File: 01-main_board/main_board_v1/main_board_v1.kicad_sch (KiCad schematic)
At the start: 2 parts, among them J1 Ethernet and USB, J4 DB44 (Analog | Digital)

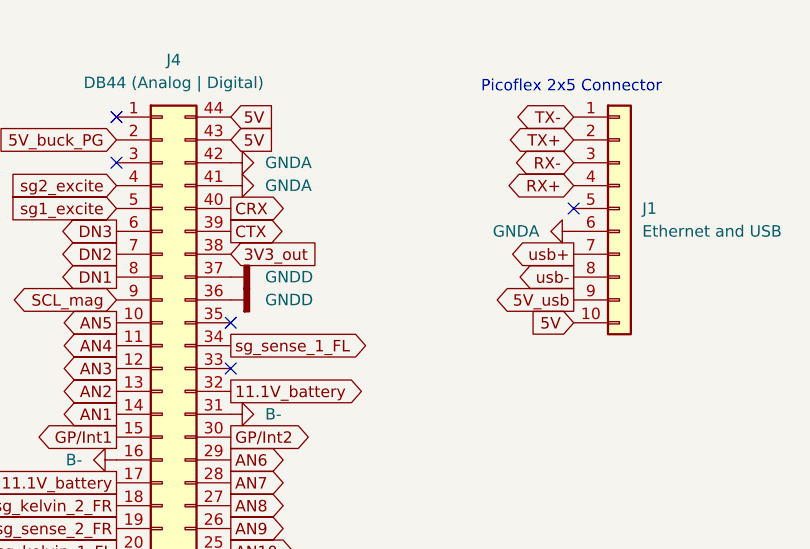
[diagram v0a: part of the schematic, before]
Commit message: Added main board footprint library
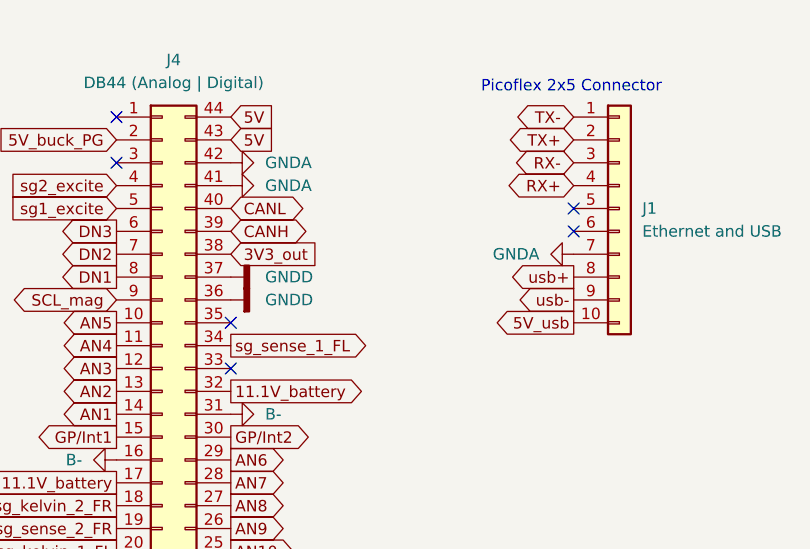
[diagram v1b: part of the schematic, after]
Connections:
- net 5V: no longer J1.10 (Pin_10)
- net 5V_usb: now also J1.10 (Pin_10); no longer J1.9 (Pin_9)
- net GNDA: now also J1.7 (Pin_7); no longer J1.6 (Pin_6)
- net usb+: now also J1.8 (Pin_8); no longer J1.7 (Pin_7)
- net usb-: now also J1.9 (Pin_9); no longer J1.8 (Pin_8)
- net CRX renamed CANL
- net CTX renamed CANH
- no-connect marks 5 -> 6
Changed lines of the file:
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@@
+	)
+	(no_connect
+		(at 111.76 43.18)
 	)
 	(no_connect
@@
 	)
 	(no_connect
+		(at 111.76 45.72)
+	)
+	(no_connect
 		(at 73.66 60.96)
 	)
@@
 		(at 60.96 38.1)
 	)
-	(no_connect
-		(at 111.76 43.18)
-	)
 	(global_label "AN7"
 		(shape output)
@@
 				)
 				(justify right)
+				(hide yes)
+			)
+		)
+	)
+	(global_label "CANL"
+		(shape bidirectional)
+		(at 73.66 43.18 0)
+		(fields_autoplaced yes)
+		(effects
+			(font
+				(size 1.27 1.27)
+			)
+			(justify left)
+		)
+		(property "Intersheetrefs" "${INTERSHEET_REFS}"
+			(at 82.4737 43.18 0)
+			(effects
+				(font
+					(size 1.27 1.27)
+				)
+				(justify left)
+				(hide yes)
+			)
+		)
+	)
+	(global_label "CANH"
+		(shape bidirectional)
+		(at 73.66 45.72 0)
+		(fields_autoplaced yes)
+		(effects
+			(font
+				(size 1.27 1.27)
+			)
+			(justify left)
+		)
+		(property "Intersheetrefs" "${INTERSHEET_REFS}"
+			(at 82.7761 45.72 0)
+			(effects
+				(font
+					(size 1.27 1.27)
+				)
+				(justify left)
 				(hide yes)
 			)
@@
 		)
 	)
-	(global_label "usb+"
-		(shape output)
-		(at 111.76 48.26 180)
-		(fields_autoplaced yes)
-		(effects
-			(font
-				(face "KiCad Font")
-				(size 1.27 1.27)
-			)
-			(justify right)
-		)
-		(property "Intersheetrefs" "${INTERSHEET_REFS}"
-			(at 103.8763 48.26 0)
-			(effects
-				(font
-					(size 1.27 1.27)
-				)
-				(justify right)
-				(hide yes)
-			)
-		)
-	)
 	(global_label "linpot_2_FR"
 		(shape output)
@@
 		)
 	)
-	(global_label "5V_usb"
-		(shape output)
-		(at 111.76 53.34 180)
-		(fields_autoplaced yes)
-		(effects
-			(font
-				(size 1.27 1.27)
-			)
-			(justify right)
-		)
-		(property "Intersheetrefs" "${INTERSHEET_REFS}"
-			(at 102.183 53.34 0)
-			(effects
-				(font
-					(size 1.27 1.27)
-				)
-				(justify right)
-				(hide yes)
-			)
-		)
-	)
 	(global_label "DN5"
 		(shape input)
@@
 		)
 	)
+	(global_label "usb+"
+		(shape output)
+		(at 111.76 50.8 180)
+		(fields_autoplaced yes)
+		(effects
+			(font
+				(face "KiCad Font")
+				(size 1.27 1.27)
+			)
+			(justify right)
+		)
+		(property "Intersheetrefs" "${INTERSHEET_REFS}"
+			(at 103.8763 50.8 0)
+			(effects
+				(font
+					(size 1.27 1.27)
+				)
+				(justify right)
+				(hide yes)
+			)
+		)
+	)
 	(global_label "11.1V_battery"
 		(shape output)
@@
 		)
 	)
-	(global_label "5V"
-		(shape input)
-		(at 111.76 55.88 180)
-		(fields_autoplaced yes)
-		(effects
-			(font
-				(size 1.27 1.27)
-			)
-			(justify right)
-		)
-		(property "Intersheetrefs" "${INTERSHEET_REFS}"
-			(at 106.4767 55.88 0)
-			(effects
-				(font
-					(size 1.27 1.27)
-				)
-				(justify right)
-				(hide yes)
-			)
-		)
-	)
 	(global_label "hallfx_2_rear"
 		(shape output)
@@
 		)
 	)
+	(global_label "usb-"
+		(shape output)
+		(at 111.76 53.34 180)
+		(fields_autoplaced yes)
+		(effects
+			(font
+				(face "KiCad Font")
+				(size 1.27 1.27)
+			)
+			(justify right)
+		)
+		(property "Intersheetrefs" "${INTERSHEET_REFS}"
+			(at 103.8763 53.34 0)
+			(effects
+				(font
+					(size 1.27 1.27)
+				)
+				(justify right)
+				(hide yes)
+			)
+		)
+	)
 	(global_label "sg_sense_1_FL"
 		(shape output)
@@
 		)
 	)
-	(global_label "CTX"
-		(shape output)
-		(at 73.66 45.72 0)
-		(fields_autoplaced yes)
-		(effects
-			(font
-				(size 1.27 1.27)
-			)
-			(justify left)
-		)
-		(property "Intersheetrefs" "${INTERSHEET_REFS}"
-			(at 80.0923 45.72 0)
-			(effects
-				(font
-					(size 1.27 1.27)
-				)
-				(justify left)
+	(global_label "5V_usb"
+		(shape output)
+		(at 111.76 55.88 180)
+		(fields_autoplaced yes)
+		(effects
+			(font
+				(size 1.27 1.27)
+			)
+			(justify right)
+		)
+		(property "Intersheetrefs" "${INTERSHEET_REFS}"
+			(at 102.183 55.88 0)
+			(effects
+				(font
+					(size 1.27 1.27)
+				)
+				(justify right)
 				(hide yes)
 			)
@@
 		(property "Intersheetrefs" "${INTERSHEET_REFS}"
 			(at 103.6116 40.64 0)
-			(effects
-				(font
-					(size 1.27 1.27)
-				)
-				(justify right)
-				(hide yes)
-			)
-		)
-	)
-	(global_label "CRX"
-		(shape output)
-		(at 73.66 43.18 0)
-		(fields_autoplaced yes)
-		(effects
-			(font
-				(size 1.27 1.27)
-			)
-			(justify left)
-		)
-		(property "Intersheetrefs" "${INTERSHEET_REFS}"
-			(at 80.3947 43.18 0)
-			(effects
-				(font
-					(size 1.27 1.27)
-				)
-				(justify left)
-				(hide yes)
-			)
-		)
-	)
-	(global_label "usb-"
-		(shape output)
-		(at 111.76 50.8 180)
-		(fields_autoplaced yes)
-		(effects
-			(font
-				(face "KiCad Font")
-				(size 1.27 1.27)
-			)
-			(justify right)
-		)
-		(property "Intersheetrefs" "${INTERSHEET_REFS}"
-			(at 103.8763 50.8 0)
 			(effects
 				(font
@@
 	(symbol
 		(lib_id "power:GND")
-		(at 111.76 45.72 270)
+		(at 111.76 48.26 270)
 		(unit 1)
 		(exclude_from_sim no)
@@
 		(fields_autoplaced yes)
 		(property "Reference" "#PWR038"
-			(at 105.41 45.72 0)
+			(at 105.41 48.26 0)
 			(effects
 				(font
@@
 		)
 		(property "Value" "GNDA"
-			(at 107.95 45.7201 90)
+			(at 107.95 48.2601 90)
 			(effects
 				(font
@@
 		)
 		(property "Footprint" ""
-			(at 111.76 45.72 0)
+			(at 111.76 48.26 0)
 			(effects
 				(font
@@
 		)
 		(property "Datasheet" ""
-			(at 111.76 45.72 0)
+			(at 111.76 48.26 0)
 			(effects
 				(font
@@
 		)
 		(property "Description" "Power symbol creates a global label with name \"GND\" , ground"
-			(at 111.76 45.72 0)
-			(effects
-				(font
+			(at 111.76 48.26 0)
+			(effects
+				(font

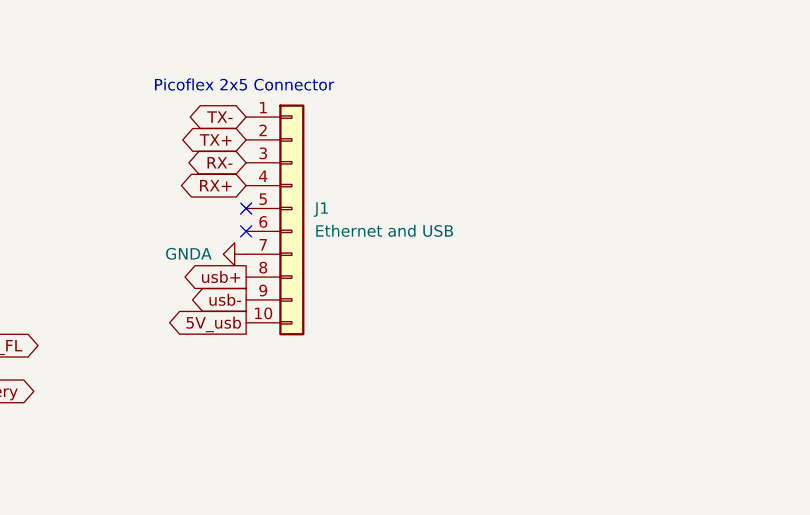
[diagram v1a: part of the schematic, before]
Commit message: Changed molex footprint
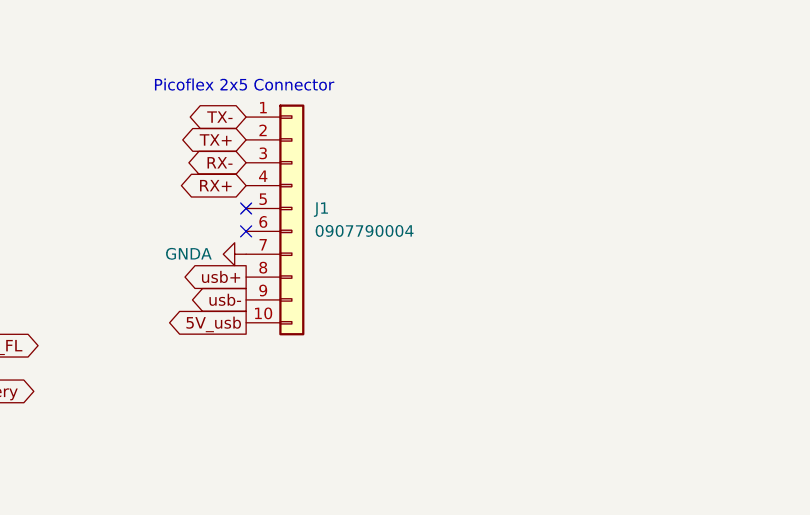
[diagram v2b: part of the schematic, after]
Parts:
- J1: value Ethernet and USB -> 0907790004; footprint Connector_Molex:Molex_Picoflex_90325-0010_2x05_P1.27mm_Vertical -> 22XT_Main:CONN_SDA-90779_10_MOL
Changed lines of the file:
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@@
 			)
 		)
-		(property "Value" "Ethernet and USB"
+		(property "Value" "0907790004"
 			(at 119.38 45.7199 0)
 			(effects
@@
 			)
 		)
-		(property "Footprint" "Connector_Molex:Molex_Picoflex_90325-0010_2x05_P1.27mm_Vertical"
+		(property "Footprint" "22XT_Main:CONN_SDA-90779_10_MOL"
 			(at 116.84 43.18 0)
 			(effects

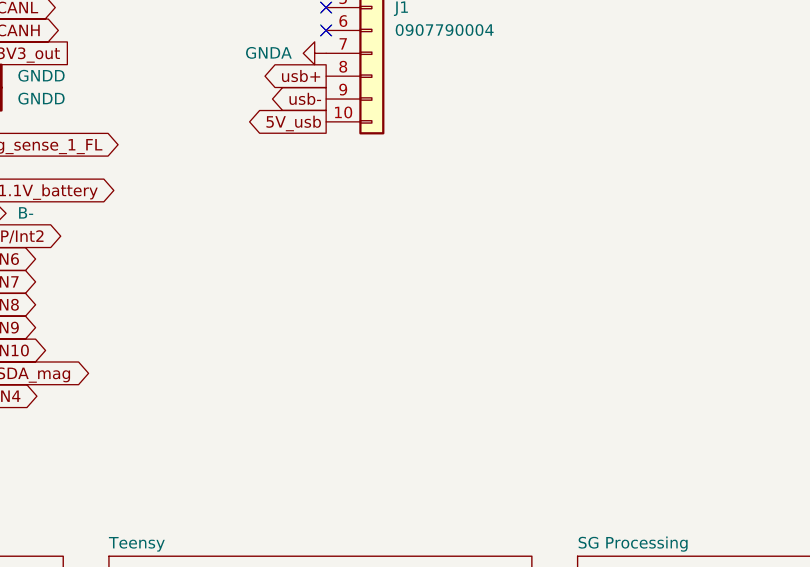
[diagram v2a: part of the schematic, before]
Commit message: new transformer layout + progress on new gnd planes
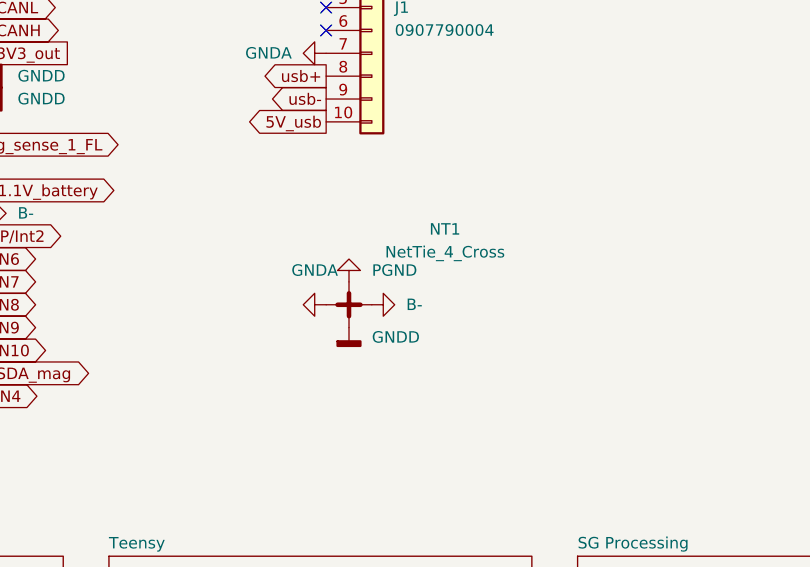
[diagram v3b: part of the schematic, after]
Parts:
- added NT1: NetTie_4_Cross, NetTie:NetTie-4_SMD_Pad0.5mm, symbol Device:NetTie_4_Cross
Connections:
- net B-: now also NT1.2
- net GNDA: now also NT1.1
- net GNDD: now also NT1.4
- new net PGND: NT1.3

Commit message: added supply test flags, gnd planes, fixed silkscreen overlaps
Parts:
- added NT2: NetTie_3_Tee, NetTie:NetTie-3_SMD_Pad0.5mm, symbol Device:NetTie_3_Tee
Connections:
- net CANH: now also J4.40 (Pin_40); no longer J4.39 (Pin_39)
- net CANL: now also J4.39 (Pin_39); no longer J4.40 (Pin_40)
- net GNDA: now also NT2.1
- net GNDD: now also NT2.2
- net PGND: now also NT2.3

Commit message: Added mezzanine edge connector
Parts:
- J1: value 0907790004 -> Mezzanine Edge; footprint 22XT_Main:CONN_SDA-90779_10_MOL -> 22XT_Main:Double Sided Mezzanine Card Edge_Edge Side
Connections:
- net GNDA: now also J1.9 (Pin_9); no longer J1.7 (Pin_7)
- net RX-: now also J1.5 (Pin_5); no longer J1.3 (Pin_3)
- net TX+: now also J1.1 (Pin_1); no longer J1.2 (Pin_2)
- net TX-: now also J1.2 (Pin_2); no longer J1.1 (Pin_1)
- net usb+: now also J1.6 (Pin_6); no longer J1.8 (Pin_8)
- net usb-: now also J1.7 (Pin_7); no longer J1.9 (Pin_9)
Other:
- note added: "Mates to Female Connector: 009159010651906"
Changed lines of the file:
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@@
 		)
 	)
-	(no_connect
-		(at 111.76 43.18)
+	(text "Mates to Female Connector: 009159010651906"
+		(exclude_from_sim no)
+		(at 119.38 60.198 0)
+		(effects
+			(font
+				(size 1.27 1.27)
+			)
+		)
 	)
 	(no_connect
@@
 	)
 	(no_connect
-		(at 111.76 45.72)
+		(at 73.66 60.96)
 	)
 	(no_connect
-		(at 73.66 60.96)
+		(at 111.76 38.1)
 	)
 	(no_connect
 		(at 73.66 55.88)
+	)
+	(no_connect
+		(at 111.76 50.8)
 	)
 	(no_connect
@@
 		)
 	)
-	(global_label "TX+"
+	(global_label "TX-"
 		(shape bidirectional)
 		(at 111.76 35.56 180)
@@
 		(property "Intersheetrefs" "${INTERSHEET_REFS}"
 			(at 54.1648 45.72 0)
+			(effects
+				(font
+					(size 1.27 1.27)
+				)
+				(justify right)
+				(hide yes)
+			)
+		)
+	)
+	(global_label "usb-"
+		(shape output)
+		(at 111.76 48.26 180)
+		(fields_autoplaced yes)
+		(effects
+			(font
+				(face "KiCad Font")
+				(size 1.27 1.27)
+			)
+			(justify right)
+		)
+		(property "Intersheetrefs" "${INTERSHEET_REFS}"
+			(at 103.8763 48.26 0)
 			(effects
 				(font
@@
 		)
 	)
-	(global_label "usb+"
-		(shape output)
-		(at 111.76 50.8 180)
-		(fields_autoplaced yes)
-		(effects
-			(font
-				(face "KiCad Font")
-				(size 1.27 1.27)
-			)
-			(justify right)
-		)
-		(property "Intersheetrefs" "${INTERSHEET_REFS}"
-			(at 103.8763 50.8 0)
-			(effects
-				(font
-					(size 1.27 1.27)
-				)
-				(justify right)
-				(hide yes)
-			)
-		)
-	)
 	(global_label "11.1V_battery"
 		(shape output)
@@
 		)
 	)
-	(global_label "hallfx_2_rear"
-		(shape output)
-		(at 34.29 78.74 180)
-		(fields_autoplaced yes)
-		(effects
-			(font
-				(face "KiCad Font")
-				(size 1.27 1.27)
-			)
-			(justify right)
-		)
-		(property "Intersheetrefs" "${INTERSHEET_REFS}"
-			(at 18.9679 78.74 0)
+	(global_label "RX+"
+		(shape bidirectional)
+		(at 111.76 40.64 180)
+		(fields_autoplaced yes)
+		(effects
+			(font
+				(size 1.27 1.27)
+			)
+			(justify right)
+		)
+		(property "Intersheetrefs" "${INTERSHEET_REFS}"
+			(at 103.6116 40.64 0)
 			(effects
 				(font
@@
 	(global_label "RX-"
 		(shape bidirectional)
-		(at 111.76 38.1 180)
-		(fields_autoplaced yes)
-		(effects
-			(font
-				(size 1.27 1.27)
-			)
-			(justify right)
-		)
-		(property "Intersheetrefs" "${INTERSHEET_REFS}"
-			(at 103.6116 38.1 0)
-			(effects
-				(font
-					(size 1.27 1.27)
-				)
-				(justify right)
-				(hide yes)
-			)
-		)
-	)
-	(global_label "usb-"
-		(shape output)
-		(at 111.76 53.34 180)
+		(at 111.76 43.18 180)
+		(fields_autoplaced yes)
+		(effects
+			(font
+				(size 1.27 1.27)
+			)
+			(justify right)
+		)
+		(property "Intersheetrefs" "${INTERSHEET_REFS}"
+			(at 103.6116 43.18 0)
+			(effects
+				(font
+					(size 1.27 1.27)
+				)
+				(justify right)
+				(hide yes)
+			)
+		)
+	)
+	(global_label "hallfx_2_rear"
+		(shape output)
+		(at 34.29 78.74 180)
 		(fields_autoplaced yes)
 		(effects
@@
 		)
 		(property "Intersheetrefs" "${INTERSHEET_REFS}"
-			(at 103.8763 53.34 0)
+			(at 18.9679 78.74 0)
 			(effects
 				(font
@@
 		)
 	)
-	(global_label "TX-"
+	(global_label "TX+"
 		(shape bidirectional)
 		(at 111.76 33.02 180)
@@
 		)
 	)
-	(global_label "RX+"
-		(shape bidirectional)
-		(at 111.76 40.64 180)
-		(fields_autoplaced yes)
-		(effects
-			(font
-				(size 1.27 1.27)
-			)
-			(justify right)
-		)
-		(property "Intersheetrefs" "${INTERSHEET_REFS}"
-			(at 103.6116 40.64 0)
+	(global_label "usb+"
+		(shape output)
+		(at 111.76 45.72 180)
+		(fields_autoplaced yes)
+		(effects
+			(font
+				(face "KiCad Font")
+				(size 1.27 1.27)
+			)
+			(justify right)
+		)
+		(property "Intersheetrefs" "${INTERSHEET_REFS}"
+			(at 103.8763 45.72 0)
 			(effects
 				(font
@@
 			)
 		)
-		(property "Value" "0907790004"
+		(property "Value" "Mezzanine Edge"
 			(at 119.38 45.7199 0)
 			(effects
@@
 			)
 		)
-		(property "Footprint" "22XT_Main:CONN_SDA-90779_10_MOL"
+		(property "Footprint" "22XT_Main:Double Sided Mezzanine Card Edge_Edge Side"
 			(at 116.84 43.18 0)
 			(effects
@@
 	(symbol
 		(lib_id "power:GND")
-		(at 111.76 48.26 270)
+		(at 111.76 53.34 270)
 		(unit 1)
 		(exclude_from_sim no)
@@
 		(fields_autoplaced yes)
 		(property "Reference" "#PWR038"
-			(at 105.41 48.26 0)
+			(at 105.41 53.34 0)
 			(effects
 				(font
@@
 		)
 		(property "Value" "GNDA"
-			(at 107.95 48.2601 90)
+			(at 107.95 53.3401 90)
 			(effects
 				(font
@@
 		)
 		(property "Footprint" ""
-			(at 111.76 48.26 0)
+			(at 111.76 53.34 0)
 			(effects
 				(font
@@
 		)
 		(property "Datasheet" ""
-			(at 111.76 48.26 0)
+			(at 111.76 53.34 0)
 			(effects
 				(font
@@
 		)
 		(property "Description" "Power symbol creates a global label with name \"GND\" , ground"
-			(at 111.76 48.26 0)
-			(effects
-				(font
+			(at 111.76 53.34 0)
+			(effects
+				(font
